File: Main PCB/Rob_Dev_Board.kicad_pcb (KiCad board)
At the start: 4 copper layers, 9 parts, among them J1 TYPE-C-31-M-12, U1 DRV8245HQRXZRQ1, U2 ESP32-S3-WROOM-1U-N16R8, U3 DRV8245HQRXZRQ1, U4 PCA9685PW_118

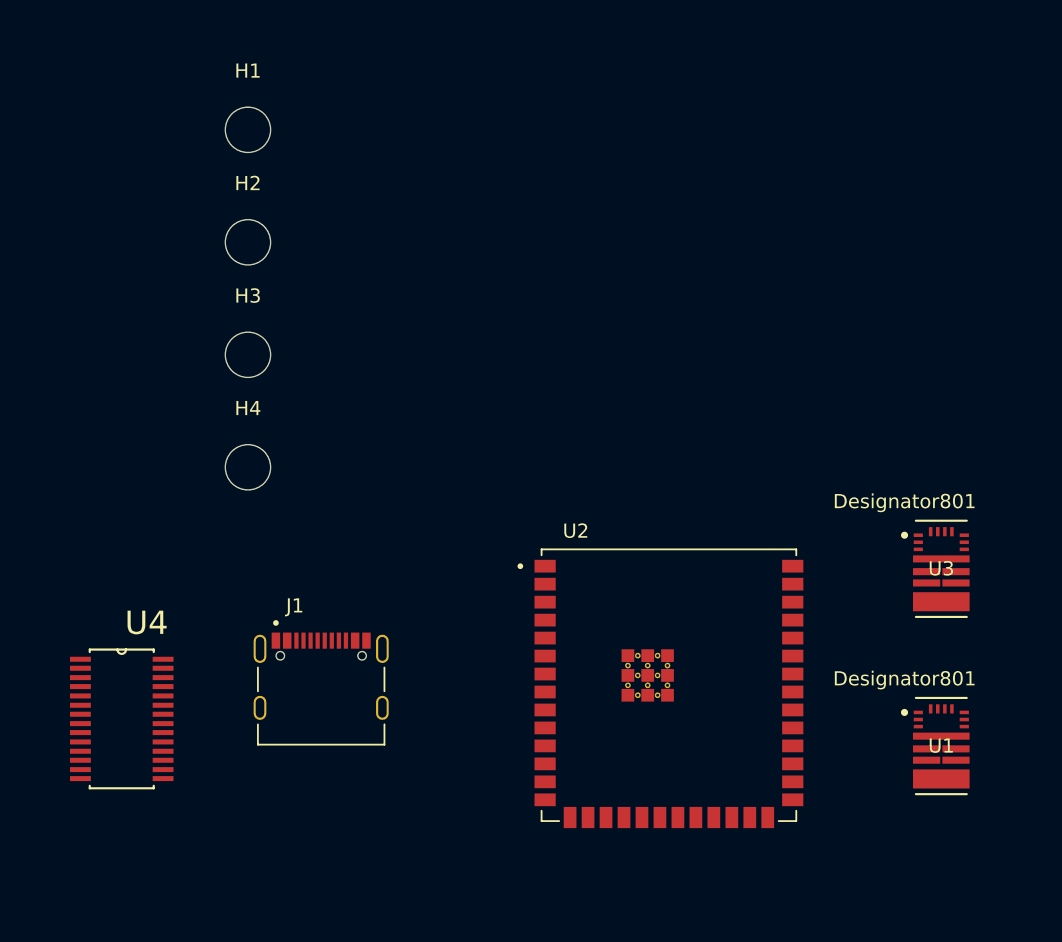
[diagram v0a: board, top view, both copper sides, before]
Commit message: Added acceler. and connector type to part library
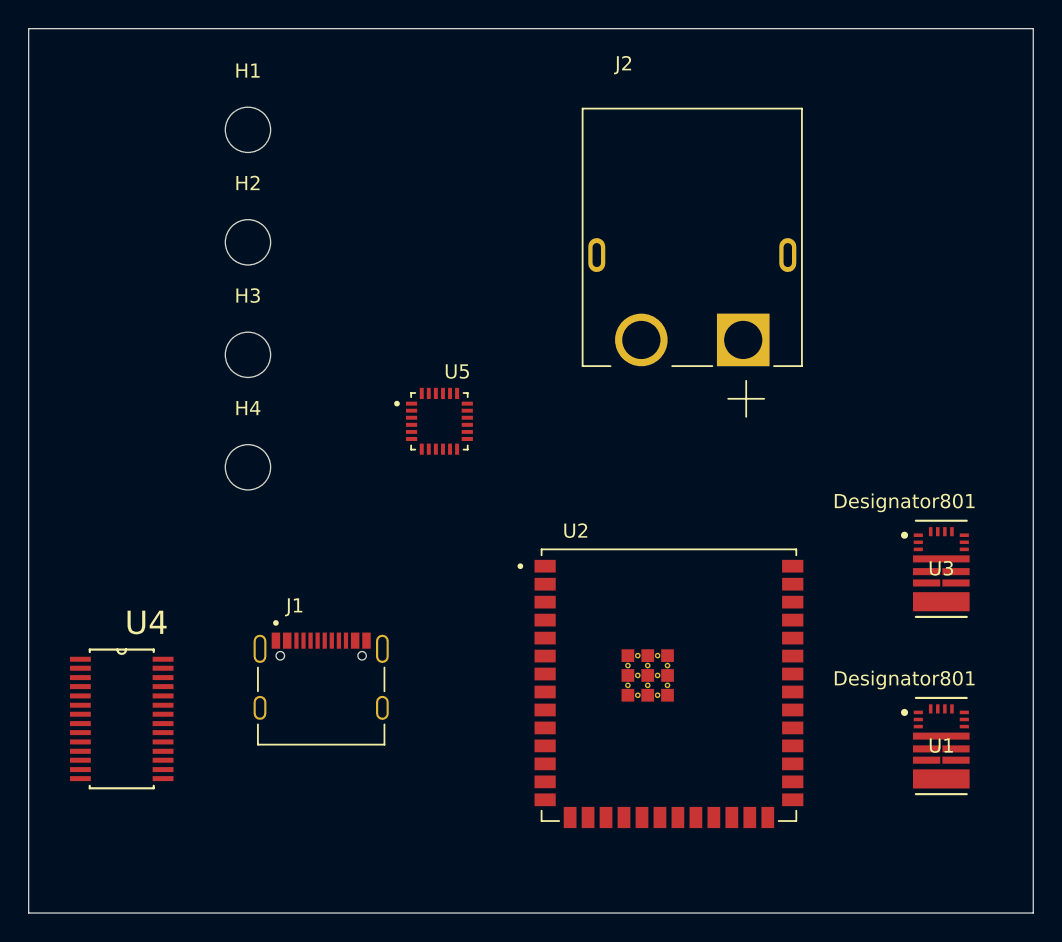
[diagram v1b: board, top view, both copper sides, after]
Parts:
- added J2: XT60PW-M, XT60PW-M Connector:AMASS_XT60PW-M, F.Cu at (85.9, 49.5)
- added U5: MPU-6050, MPU-6050 Accelerometer:QFN50P400X400X95-24N, F.Cu at (68.0, 61.2)
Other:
- board outline added: 71 x 62.5 mm

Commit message: Testing
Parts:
- added J10: XT60PW-M, XT60PW-M Connector:AMASS_XT60PW-M, F.Cu at (184.0, 100.0)
- added J11: XT60PW-M, XT60PW-M Connector:AMASS_XT60PW-M, F.Cu at (179.0, 79.5)
- added J12: XT60PW-M, XT60PW-M Connector:AMASS_XT60PW-M, F.Cu at (161.5, 79.5)
- added J3: XT60PW-M, XT60PW-M Connector:AMASS_XT60PW-M, F.Cu at (105.0, 79.0)
- added J4: XT60PW-M, XT60PW-M Connector:AMASS_XT60PW-M, F.Cu at (100.0, 99.2)
- added J5: XT60PW-M, XT60PW-M Connector:AMASS_XT60PW-M, F.Cu at (100.0, 118.2)
- added J6: XT60PW-M, XT60PW-M Connector:AMASS_XT60PW-M, F.Cu at (100.0, 137.2)
- added J7: XT60PW-M, XT60PW-M Connector:AMASS_XT60PW-M, F.Cu at (184.0, 138.2)
- added J8: XT60PW-M, XT60PW-M Connector:AMASS_XT60PW-M, F.Cu at (123.5, 79.0)
- added J9: XT60PW-M, XT60PW-M Connector:AMASS_XT60PW-M, F.Cu at (184.0, 119.8)
- moved H1 131.3 mm to (161.0, 117.5)
- moved H4 111.2 mm to (160.5, 98.0)
- moved J1 110.3 mm to (146.8, 149.2)
- moved U4 105.5 mm to (146.5, 113.0), turned to 90 degrees
- moved H2 103.4 mm to (132.0, 117.0)
- moved U5 94.1 mm to (131.8, 130.5)
- moved U1 87.3 mm to (172.2, 138.0), turned to 90 degrees
- moved H3 87.2 mm to (131.5, 97.5)
- moved U2 81.6 mm to (146.4, 132.8), turned to 180 degrees
- moved U3 66.3 mm to (113.4, 137.2), turned to -90 degrees
- moved J2 63.8 mm to (142.5, 79.0)
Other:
- board size 71 x 62.5 mm -> 90 x 76 mm

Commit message: cho
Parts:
- moved J5 13.3 mm to (87.0, 115.2)
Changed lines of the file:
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@@
 	(footprint "XT60PW-M Connector:AMASS_XT60PW-M"
 		(layer "F.Cu")
-		(at 100 118.25 90)
+		(at 87 115.25 90)
 		(property "Reference" "J5"
 			(at -4.8236 -13.51498 90)

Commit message: testing
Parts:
- moved J11 19.0 mm to (193.8, 67.5)
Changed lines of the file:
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@@
 	(footprint "XT60PW-M Connector:AMASS_XT60PW-M"
 		(layer "F.Cu")
-		(at 179 79.5)
+		(at 193.75 67.5)
 		(property "Reference" "J11"
 			(at -4.8236 -13.51498 0)
